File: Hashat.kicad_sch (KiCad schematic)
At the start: 0 parts

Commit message: more schematic
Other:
- sheet BM1397 ports: added BI, CI, RO, RST; removed none
- sheet RPi ports: added BI, CI, RO, RST; removed none
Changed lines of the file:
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@@
+    (stroke (width 0) (type default))
+  )
+  (wire (pts (xy 96.52 127) (xy 154.94 127))
     (stroke (width 0) (type default))
   )
@@
     (stroke (width 0) (type default))
   )
+  (wire (pts (xy 96.52 121.92) (xy 149.86 121.92))
+    (stroke (width 0) (type default))
+  )
+  (wire (pts (xy 152.4 90.17) (xy 152.4 124.46))
+    (stroke (width 0) (type default))
+  )
   (wire (pts (xy 97.79 64.77) (xy 103.505 64.77))
     (stroke (width 0) (type default))
@@
     (stroke (width 0) (type default))
   )
-  (wire (pts (xy 96.52 144.145) (xy 113.03 144.145))
+  (wire (pts (xy 96.52 161.29) (xy 114.935 161.29))
     (stroke (width 0) (type default))
   )
@@
     (stroke (width 0) (type default))
   )
+  (wire (pts (xy 154.94 92.71) (xy 161.925 92.71))
+    (stroke (width 0) (type default))
+  )
   (wire (pts (xy 156.21 80.645) (xy 161.925 80.645))
     (stroke (width 0) (type default))
   )
-  (wire (pts (xy 113.03 144.145) (xy 113.03 113.03))
+  (wire (pts (xy 114.935 161.29) (xy 114.935 137.16))
     (stroke (width 0) (type default))
   )
@@
     (stroke (width 0) (type default))
   )
-  (wire (pts (xy 127.635 151.765) (xy 127.635 76.2))
-    (stroke (width 0) (type default))
-  )
-  (wire (pts (xy 96.52 151.765) (xy 127.635 151.765))
+  (wire (pts (xy 127.635 168.91) (xy 127.635 76.2))
+    (stroke (width 0) (type default))
+  )
+  (wire (pts (xy 96.52 168.91) (xy 127.635 168.91))
     (stroke (width 0) (type default))
   )
@@
     (stroke (width 0) (type default))
   )
-  (wire (pts (xy 113.03 113.03) (xy 96.52 113.03))
-    (stroke (width 0) (type default))
-  )
-  (wire (pts (xy 96.52 154.305) (xy 130.81 154.305))
-    (stroke (width 0) (type default))
-  )
-  (wire (pts (xy 114.935 110.49) (xy 114.935 146.685))
+  (wire (pts (xy 114.935 137.16) (xy 96.52 137.16))
+    (stroke (width 0) (type default))
+  )
+  (wire (pts (xy 96.52 171.45) (xy 130.81 171.45))
+    (stroke (width 0) (type default))
+  )
+  (wire (pts (xy 118.11 134.62) (xy 118.11 163.83))
+    (stroke (width 0) (type default))
+  )
+  (wire (pts (xy 161.925 95.25) (xy 156.845 95.25))
+    (stroke (width 0) (type default))
+  )
+  (wire (pts (xy 161.925 90.17) (xy 152.4 90.17))
+    (stroke (width 0) (type default))
+  )
+  (wire (pts (xy 154.94 127) (xy 154.94 92.71))
     (stroke (width 0) (type default))
   )
@@
     (stroke (width 0) (type default))
   )
-  (wire (pts (xy 96.52 110.49) (xy 114.935 110.49))
+  (wire (pts (xy 96.52 134.62) (xy 118.11 134.62))
     (stroke (width 0) (type default))
   )
@@
     (stroke (width 0) (type default))
   )
-  (wire (pts (xy 114.935 146.685) (xy 96.52 146.685))
-    (stroke (width 0) (type default))
-  )
-  (wire (pts (xy 130.81 154.305) (xy 130.81 73.66))
+  (wire (pts (xy 149.86 87.63) (xy 161.925 87.63))
+    (stroke (width 0) (type default))
+  )
+  (wire (pts (xy 118.11 163.83) (xy 96.52 163.83))
+    (stroke (width 0) (type default))
+  )
+  (wire (pts (xy 156.845 129.54) (xy 96.52 129.54))
+    (stroke (width 0) (type default))
+  )
+  (wire (pts (xy 130.81 171.45) (xy 130.81 73.66))
+    (stroke (width 0) (type default))
+  )
+  (wire (pts (xy 152.4 124.46) (xy 96.52 124.46))
     (stroke (width 0) (type default))
   )
@@
     (stroke (width 0) (type default))
   )
-  (wire (pts (xy 96.52 137.795) (xy 104.14 137.795))
-    (stroke (width 0) (type default))
-  )
-  (wire (pts (xy 96.52 140.335) (xy 104.14 140.335))
+  (wire (pts (xy 96.52 154.94) (xy 104.14 154.94))
+    (stroke (width 0) (type default))
+  )
+  (wire (pts (xy 149.86 121.92) (xy 149.86 87.63))
+    (stroke (width 0) (type default))
+  )
+  (wire (pts (xy 156.845 95.25) (xy 156.845 129.54))
+    (stroke (width 0) (type default))
+  )
+  (wire (pts (xy 96.52 157.48) (xy 104.14 157.48))
     (stroke (width 0) (type default))
   )
@@
     (effects (font (size 1.27 1.27)) (justify left bottom))
   )
-  (label "5V" (at 100.33 140.335 0) (fields_autoplaced)
+  (label "5V" (at 100.33 157.48 0) (fields_autoplaced)
     (effects (font (size 1.27 1.27)) (justify left bottom))
   )
@@
     (effects (font (size 1.27 1.27)) (justify left bottom))
   )
-  (label "3V3" (at 99.695 137.795 0) (fields_autoplaced)
+  (label "3V3" (at 99.695 154.94 0) (fields_autoplaced)
     (effects (font (size 1.27 1.27)) (justify left bottom))
   )
@@
     )
     (pin "3V3" output (at 161.925 83.185 180)
+      (effects (font (size 1.27 1.27)) (justify left))
+    )
+    (pin "CI" output (at 161.925 92.71 180)
+      (effects (font (size 1.27 1.27)) (justify left))
+    )
+    (pin "RO" input (at 161.925 87.63 180)
+      (effects (font (size 1.27 1.27)) (justify left))
+    )
+    (pin "BI" output (at 161.925 95.25 180)
+      (effects (font (size 1.27 1.27)) (justify left))
+    )
+    (pin "RST" output (at 161.925 90.17 180)
       (effects (font (size 1.27 1.27)) (justify left))
     )
@@
     )
   )
-  (sheet (at 57.785 97.79) (size 38.735 27.94) (fields_autoplaced)
+  (sheet (at 57.785 97.79) (size 38.735 43.18) (fields_autoplaced)
     (stroke (width 0.1524) (type solid))
     (fill (color 255 255 194 1.0000))
@@
       (effects (font (size 1.27 1.27)) (justify left bottom))
     )
-    (property "Sheetfile" "bm1397.kicad_sch" (at 57.785 126.3146 0)
+    (property "Sheetfile" "bm1397.kicad_sch" (at 57.785 141.5546 0)
       (effects (font (size 1.27 1.27)) (justify left top))
     )
@@
       (effects (font (size 1.27 1.27)) (justify right))
     )
-    (pin "TEMP_N" input (at 96.52 110.49 0)
-      (effects (font (size 1.27 1.27)) (justify right))
-    )
-    (pin "TEMP_P" input (at 96.52 113.03 0)
+    (pin "TEMP_N" input (at 96.52 134.62 0)
+      (effects (font (size 1.27 1.27)) (justify right))
+    )
+    (pin "TEMP_P" input (at 96.52 137.16 0)
+      (effects (font (size 1.27 1.27)) (justify right))
+    )
+    (pin "RO" output (at 96.52 121.92 0)
+      (effects (font (size 1.27 1.27)) (justify right))
+    )
+    (pin "RST" input (at 96.52 124.46 0)
+      (effects (font (size 1.27 1.27)) (justify right))
+    )
+    (pin "CI" input (at 96.52 127 0)
+      (effects (font (size 1.27 1.27)) (justify right))
+    )
+    (pin "BI" input (at 96.52 129.54 0)
       (effects (font (size 1.27 1.27)) (justify right))
     )
@@
     )
   )
-  (sheet (at 57.785 134.62) (size 38.735 27.94) (fields_autoplaced)
-    (stroke (width 0.1524) (type solid))
-    (fill (color 255 255 194 1.0000))
-    (property "Sheetname" "Fan" (at 57.785 133.9084 0)
-      (effects (font (size 1.27 1.27)) (justify left bottom))
-    )
-    (property "Sheetfile" "fan.kicad_sch" (at 57.785 163.1446 0)
-      (effects (font (size 1.27 1.27)) (justify left top))
-    )
-    (pin "5V" input (at 96.52 140.335 0)
-      (effects (font (size 1.27 1.27)) (justify right))
-    )
-    (pin "TEMP_P" input (at 96.52 144.145 0)
-      (effects (font (size 1.27 1.27)) (justify right))
-    )
-    (pin "TEMP_N" input (at 96.52 146.685 0)
-      (effects (font (size 1.27 1.27)) (justify right))
-    )
-    (pin "3V3" input (at 96.52 137.795 0)
-      (effects (font (size 1.27 1.27)) (justify right))
-    )
-    (pin "SDA" input (at 96.52 151.765 0)
-      (effects (font (size 1.27 1.27)) (justify right))
-    )
-    (pin "SCL" input (at 96.52 154.305 0)
-      (effects (font (size 1.27 1.27)) (justify right))
-    )
+  (sheet (at 57.785 151.765) (size 38.735 27.94) (fields_autoplaced)
+    (stroke (width 0.1524) (type solid))
+    (fill (color 255 255 194 1.0000))
+    (property "Sheetname" "Fan" (at 57.785 151.0534 0)
+      (effects (font (size 1.27 1.27)) (justify left bottom))
+    )
+    (property "Sheetfile" "fan.kicad_sch" (at 57.785 180.2896 0)
+      (effects (font (size 1.27 1.27)) (justify left top))
+    )
+    (pin "5V" input (at 96.52 157.48 0)
+      (effects (font (size 1.27 1.27)) (justify right))
+    )
+    (pin "TEMP_P" input (at 96.52 161.29 0)
+      (effects (font (size 1.27 1.27)) (justify right))
+    )
+    (pin "TEMP_N" input (at 96.52 163.83 0)
+      (effects (font (size 1.27 1.27)) (justify right))
+    )
+    (pin "3V3" input (at 96.52 154.94 0)
+      (effects (font (size 1.27 1.27)) (justify right))
+    )
+    (pin "SDA" input (at 96.52 168.91 0)
+      (effects (font (size 1.27 1.27)) (justify right))
+    )
+    (pin "SCL" input (at 96.52 171.45 0)
+      (effects (font (size 1.27 1.27)) (justify right))
+    )

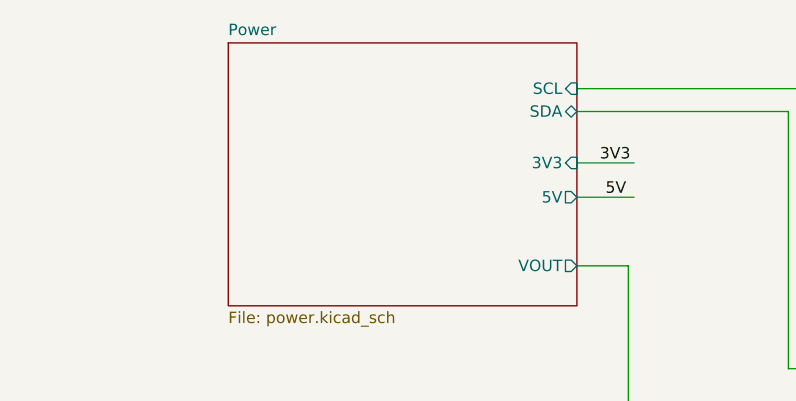
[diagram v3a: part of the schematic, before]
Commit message: more schematic. added the barrel power connector
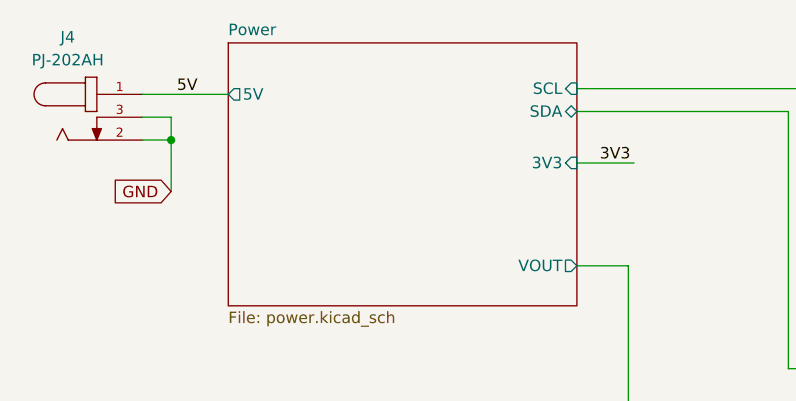
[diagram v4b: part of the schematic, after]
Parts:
- added J4: PJ-202AH, bitaxe:CUI_PJ-202AH, symbol Hashat:PJ-202AH
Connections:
- net 5V: now also J4.1
- new net GND: J4.2, J4.3
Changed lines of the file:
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@@
   (junction (at 127.635 76.2) (diameter 0) (color 0 0 0 0)
   )
+  (junction (at 52.705 50.8) (diameter 0) (color 0 0 0 0)
+  )
   (wire (pts (xy 97.79 53.34) (xy 104.14 53.34))
     (stroke (width 0) (type default))
   )
+  (wire (pts (xy 52.705 48.26) (xy 52.705 50.8))
+    (stroke (width 0) (type default))
+  )
   (wire (pts (xy 96.52 127) (xy 154.94 127))
     (stroke (width 0) (type default))
@@
     (stroke (width 0) (type default))
   )
+  (wire (pts (xy 49.53 48.26) (xy 52.705 48.26))
+    (stroke (width 0) (type default))
+  )
   (wire (pts (xy 154.94 92.71) (xy 161.925 92.71))
     (stroke (width 0) (type default))
@@
     (stroke (width 0) (type default))
   )
+  (wire (pts (xy 52.705 50.8) (xy 52.705 56.515))
+    (stroke (width 0) (type default))
+  )
   (wire (pts (xy 127.635 168.91) (xy 127.635 76.2))
     (stroke (width 0) (type default))
@@
     (stroke (width 0) (type default))
   )
+  (wire (pts (xy 49.53 45.72) (xy 59.055 45.72))
+    (stroke (width 0) (type default))
+  )
   (wire (pts (xy 154.94 127) (xy 154.94 92.71))
     (stroke (width 0) (type default))
@@
     (stroke (width 0) (type default))
   )
-  (wire (pts (xy 97.79 57.15) (xy 104.14 57.15))
-    (stroke (width 0) (type default))
-  )
   (wire (pts (xy 96.52 134.62) (xy 118.11 134.62))
     (stroke (width 0) (type default))
@@
     (stroke (width 0) (type default))
   )
+  (wire (pts (xy 49.53 50.8) (xy 52.705 50.8))
+    (stroke (width 0) (type default))
+  )
   (wire (pts (xy 96.52 154.94) (xy 104.14 154.94))
     (stroke (width 0) (type default))
@@
     (effects (font (size 1.27 1.27)) (justify left bottom))
   )
+  (label "5V" (at 53.34 45.72 0) (fields_autoplaced)
+    (effects (font (size 1.27 1.27)) (justify left bottom))
+  )
   (label "3V3" (at 158.115 83.185 0) (fields_autoplaced)
     (effects (font (size 1.27 1.27)) (justify left bottom))
   )
-  (label "5V" (at 100.965 57.15 0) (fields_autoplaced)
-    (effects (font (size 1.27 1.27)) (justify left bottom))
-  )
   (label "3V3" (at 99.695 154.94 0) (fields_autoplaced)
     (effects (font (size 1.27 1.27)) (justify left bottom))
+  )
+  (global_label "GND" (shape input) (at 52.705 56.515 180) (fields_autoplaced)
+    (effects (font (size 1.27 1.27)) (justify right))
+    (property "Intersheetrefs" "${INTERSHEET_REFS}" (at 46.5829 56.515 0)
+      (effects (font (size 1.27 1.27)) (justify right) hide)
+    )
+  )
+  (symbol (lib_id "Hashat:PJ-202AH") (at 44.45 48.26 0) (unit 1)
+    (in_bom yes) (on_board yes) (dnp no) (fields_autoplaced)
+    (property "Reference" "J4" (at 41.2142 39.37 0)
+      (effects (font (size 1.27 1.27)))
+    )
+    (property "Value" "PJ-202AH" (at 41.2142 41.91 0)
+      (effects (font (size 1.27 1.27)))
+    )
+    (property "Footprint" "bitaxe:CUI_PJ-202AH" (at 46.99 41.91 0)
+      (effects (font (size 1.27 1.27)) (justify bottom) hide)
+    )
+    (property "Datasheet" "https://www.cuidevices.com/product/resource/pj-202ah.pdf" (at 44.45 48.26 0)
+      (effects (font (size 1.27 1.27)) hide)
+    )
+    (property "PARTNO" "PJ-202AH" (at 44.45 48.26 0)
+      (effects (font (size 1.27 1.27)) hide)
+    )
+    (property "DK" "CP-202AH-ND" (at 44.45 48.26 0)
+      (effects (font (size 1.27 1.27)) hide)
+    )
+    (pin "1")
+    (pin "2")
+    (pin "3")
+    (instances
+      (project "Hashat"
+        (path "/00740941-7ad8-466a-a267-188591e2b5c4"
+          (reference "J4") (unit 1)
+        )
+      )
+    )
   )
   (sheet (at 161.925 69.85) (size 25.4 31.75) (fields_autoplaced)
@@
       (effects (font (size 1.27 1.27)) (justify right))
     )
-    (pin "5V" output (at 97.79 57.15 0)
-      (effects (font (size 1.27 1.27)) (justify right))
-    )
-    (instances
+    (pin "5V" output (at 59.055 45.72 180)
+      (effects (font (size 1.27 1.27)) (justify left))
+    )
+    (instances

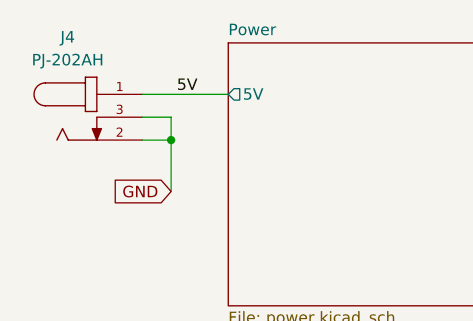
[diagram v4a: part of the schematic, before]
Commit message: cleared up some part reference designator madness
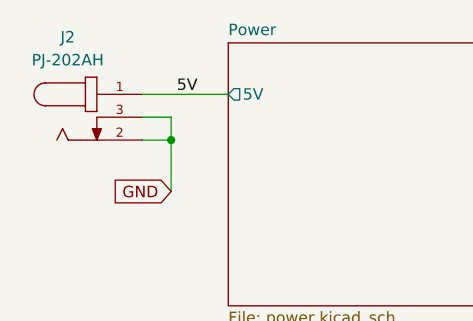
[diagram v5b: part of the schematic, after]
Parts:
- renumbered J4 to J2
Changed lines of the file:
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@@
   (symbol (lib_id "Hashat:PJ-202AH") (at 44.45 48.26 0) (unit 1)
     (in_bom yes) (on_board yes) (dnp no) (fields_autoplaced)
-    (property "Reference" "J4" (at 41.2142 39.37 0)
+    (property "Reference" "J2" (at 41.2142 39.37 0)
       (effects (font (size 1.27 1.27)))
     )
@@
       (project "Hashat"
         (path "/00740941-7ad8-466a-a267-188591e2b5c4"
-          (reference "J4") (unit 1)
+          (reference "J2") (unit 1)
         )
       )

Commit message: swapped out the VCCIO LDOs for some LCSC versions
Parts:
- removed J2: PJ-202AH, bitaxe:CUI_PJ-202AH, symbol Hashat:PJ-202AH
- added DC1: DC-044K-D025, lcsc:DC-IN-TH_DC-044K-D025, symbol lcsc:DC-044K-D025
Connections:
- net 5V: now also DC1.4
- net GND: now also DC1.1, DC1.2, DC1.3, DC1.6
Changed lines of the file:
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@@
     (date "2023-04-21")
   )
+  (junction (at 52.705 48.26) (diameter 0) (color 0 0 0 0)
+  )
   (junction (at 130.81 73.66) (diameter 0) (color 0 0 0 0)
   )
+  (junction (at 52.705 50.8) (diameter 0) (color 0 0 0 0)
+  )
   (junction (at 127.635 76.2) (diameter 0) (color 0 0 0 0)
   )
-  (junction (at 52.705 50.8) (diameter 0) (color 0 0 0 0)
+  (junction (at 52.705 53.34) (diameter 0) (color 0 0 0 0)
   )
   (wire (pts (xy 97.79 53.34) (xy 104.14 53.34))
@@
     (stroke (width 0) (type default))
   )
-  (wire (pts (xy 52.705 50.8) (xy 52.705 56.515))
-    (stroke (width 0) (type default))
-  )
   (wire (pts (xy 127.635 168.91) (xy 127.635 76.2))
     (stroke (width 0) (type default))
@@
     (stroke (width 0) (type default))
   )
+  (wire (pts (xy 49.53 43.18) (xy 52.705 43.18))
+    (stroke (width 0) (type default))
+  )
   (wire (pts (xy 96.52 106.045) (xy 103.505 106.045))
     (stroke (width 0) (type default))
@@
     (stroke (width 0) (type default))
   )
+  (wire (pts (xy 49.53 50.8) (xy 52.705 50.8))
+    (stroke (width 0) (type default))
+  )
   (wire (pts (xy 96.52 171.45) (xy 130.81 171.45))
     (stroke (width 0) (type default))
@@
     (stroke (width 0) (type default))
   )
+  (wire (pts (xy 49.53 53.34) (xy 52.705 53.34))
+    (stroke (width 0) (type default))
+  )
   (wire (pts (xy 161.925 90.17) (xy 152.4 90.17))
     (stroke (width 0) (type default))
@@
     (stroke (width 0) (type default))
   )
+  (wire (pts (xy 52.705 53.34) (xy 52.705 56.515))
+    (stroke (width 0) (type default))
+  )
+  (wire (pts (xy 52.705 50.8) (xy 52.705 53.34))
+    (stroke (width 0) (type default))
+  )
   (wire (pts (xy 96.52 134.62) (xy 118.11 134.62))
     (stroke (width 0) (type default))
@@
     (stroke (width 0) (type default))
   )
-  (wire (pts (xy 49.53 50.8) (xy 52.705 50.8))
+  (wire (pts (xy 52.705 43.18) (xy 52.705 48.26))
     (stroke (width 0) (type default))
   )
@@
     )
   )
-  (symbol (lib_id "Hashat:PJ-202AH") (at 44.45 48.26 0) (unit 1)
-    (in_bom yes) (on_board yes) (dnp no) (fields_autoplaced)
-    (property "Reference" "J2" (at 41.2142 39.37 0)
+  (symbol (lib_id "lcsc:DC-044K-D025") (at 41.91 48.26 0) (unit 1)
+    (in_bom yes) (on_board yes) (dnp no)
+    (property "Reference" "DC1" (at 35.56 41.91 0)
       (effects (font (size 1.27 1.27)))
     )
-    (property "Value" "PJ-202AH" (at 41.2142 41.91 0)
+    (property "Value" "DC-044K-D025" (at 31.75 54.61 0)
       (effects (font (size 1.27 1.27)))
     )
-    (property "Footprint" "bitaxe:CUI_PJ-202AH" (at 46.99 41.91 0)
-      (effects (font (size 1.27 1.27)) (justify bottom) hide)
-    )
-    (property "Datasheet" "https://www.cuidevices.com/product/resource/pj-202ah.pdf" (at 44.45 48.26 0)
-      (effects (font (size 1.27 1.27)) hide)
-    )
-    (property "PARTNO" "PJ-202AH" (at 44.45 48.26 0)
-      (effects (font (size 1.27 1.27)) hide)
-    )
-    (property "DK" "CP-202AH-ND" (at 44.45 48.26 0)
+    (property "Footprint" "lcsc:DC-IN-TH_DC-044K-D025" (at 41.91 60.96 0)
+      (effects (font (size 1.27 1.27)) hide)
+    )
+    (property "Datasheet" "" (at 41.91 48.26 0)
+      (effects (font (size 1.27 1.27)) hide)
+    )
+    (property "Manufacturer" "G-Switch" (at 41.91 63.5 0)
+      (effects (font (size 1.27 1.27)) hide)
+    )
+    (property "LCSC Part" "C963204" (at 41.91 66.04 0)
+      (effects (font (size 1.27 1.27)) hide)
+    )
+    (property "JLC Part" "Extended Part" (at 41.91 68.58 0)
       (effects (font (size 1.27 1.27)) hide)
     )
@@
     (pin "2")
     (pin "3")
+    (pin "4")
+    (pin "6")
     (instances
       (project "Hashat"
         (path "/00740941-7ad8-466a-a267-188591e2b5c4"
-          (reference "J2") (unit 1)
+          (reference "DC1") (unit 1)
         )
       )
